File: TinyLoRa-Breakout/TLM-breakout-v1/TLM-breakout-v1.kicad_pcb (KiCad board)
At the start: 2 copper layers, 22.9 x 50.8 mm, 46 parts, among them J1 SMA-Edge-Mount, J2 U.FL-R-SMT-1, J3 JST_PH, J4 USB_B_Micro, J5 Cortex_JTAG_SWD_10pin, SW3 RESET, U1 TLM01, U2 MCP73831-2-OT, U3 TPS3839DBZ, U4 S-1313C33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

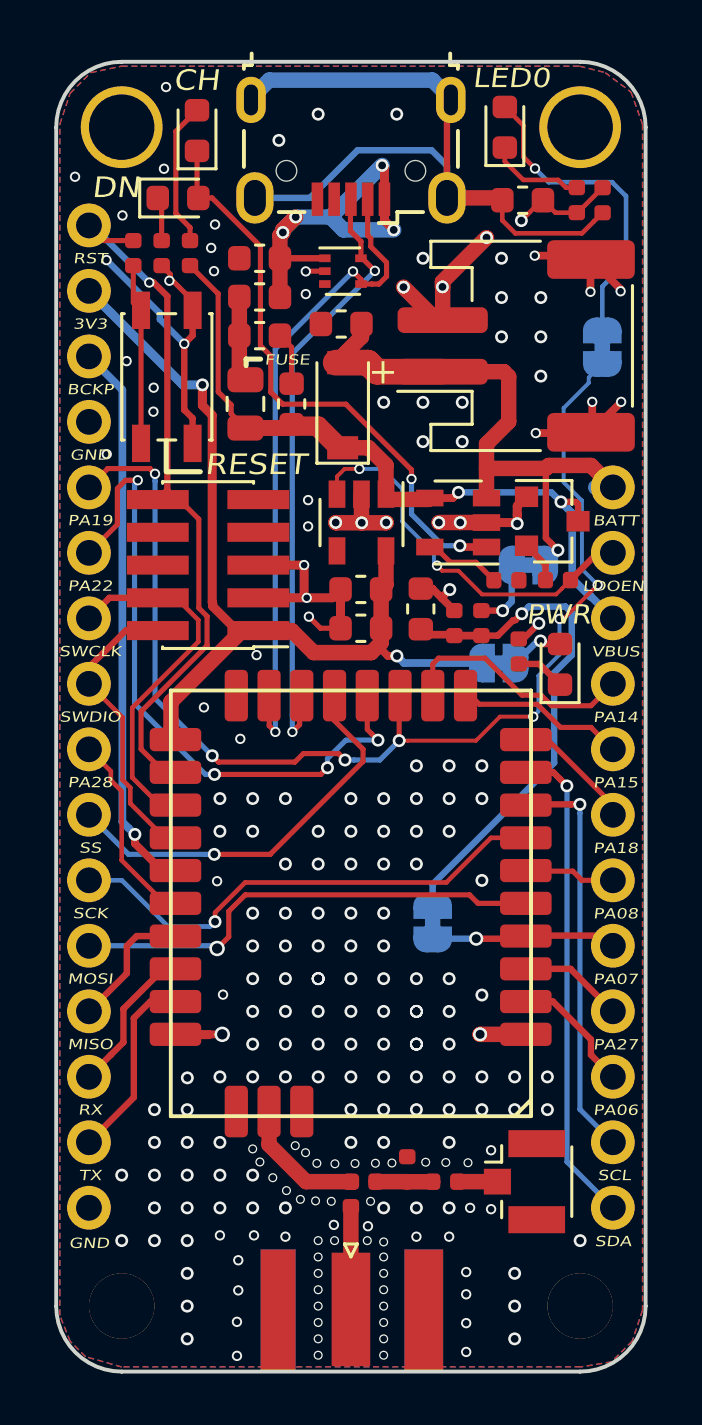
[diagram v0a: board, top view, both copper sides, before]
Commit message: BOMs added
BOMs for TinyLoRa and its breakout added
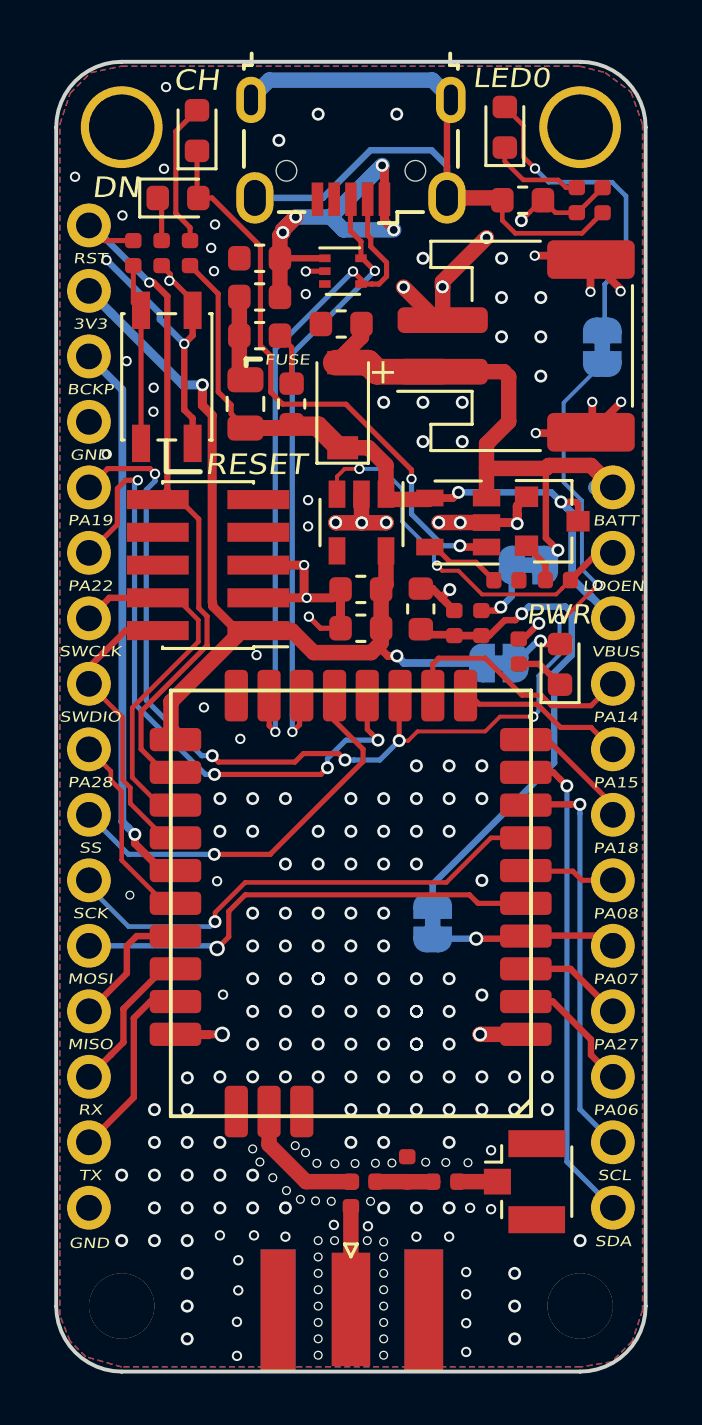
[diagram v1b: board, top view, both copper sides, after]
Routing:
- net PA19_PWM_T0_W3: track 46.2 -> 46.8 mm
- net GND: vias 221 -> 222
